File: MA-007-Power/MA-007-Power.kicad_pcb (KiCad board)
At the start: 2 copper layers, 61 x 41.9 mm, 14 parts, among them J1 Conn_01x02, J2 Conn_01x03, J3 Power Out

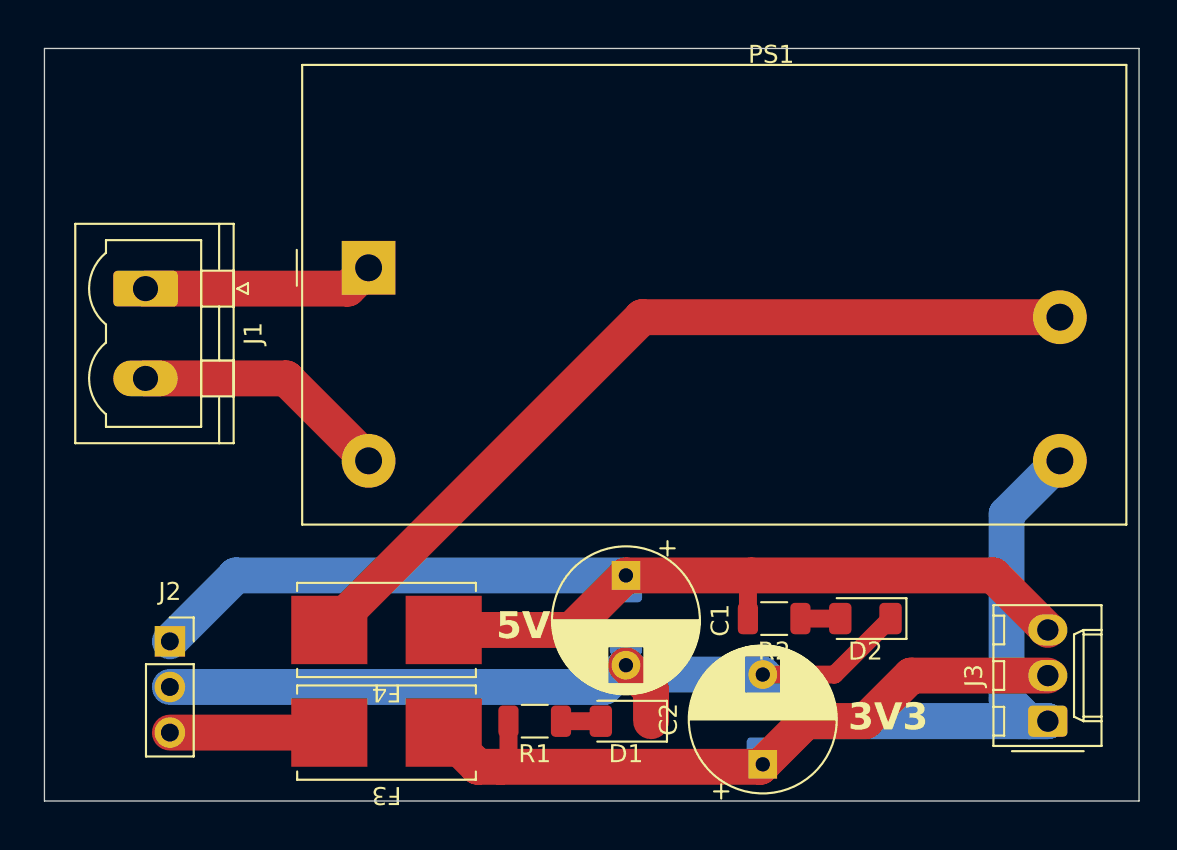
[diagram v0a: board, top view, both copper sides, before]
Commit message: Finished up PCBs, added stencil
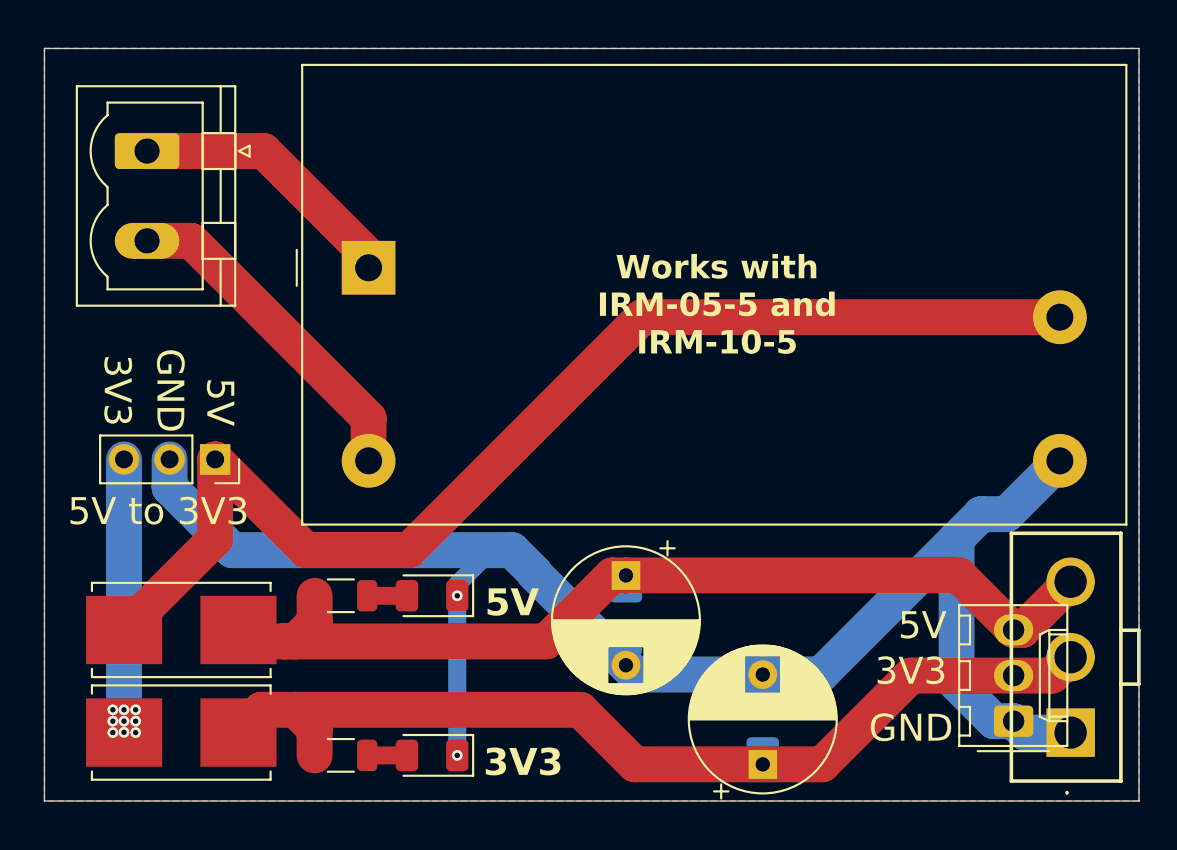
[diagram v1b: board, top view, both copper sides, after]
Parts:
- added J4: 43242-0005, Molex_MiniFitJr_1x3:Molex_MiniFitJr_1x3_PCB, F.Cu at (159.4, 94.0)
- moved D2 24.2 mm to (123.8, 86.4)
- moved R2 24.2 mm to (118.7, 86.4)
- moved F3 11.4 mm to (109.9, 94.0)
- moved F4 11.4 mm to (109.9, 88.3)
- moved D1 11.0 mm to (123.8, 95.2)
- moved R1 11.0 mm to (118.7, 95.2)
- moved J2 10.4 mm to (111.7, 78.8), turned to -90 degrees
- moved J1 7.66 mm to (108.0, 61.6)
- moved J3 1.91 mm to (156.2, 93.3)
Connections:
- J2 pad 1: /5V -> /5V_PRE
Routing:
- net /5V_PRE: track 47.9 -> 66.1 mm
- net /3V3: track 39.3 -> 53.6 mm
- net /5V: track 65.6 -> 54.1 mm
- net GND: track 80.1 -> 88.3 mm, vias 0 -> 2
- net Net-(J2-Pin_3): track 8.88 -> 15.2 mm, vias 0 -> 9
- net Net-(J1-Pin_2): track 14.3 -> 18.8 mm
- net Net-(J1-Pin_1): track 12.9 -> 15.4 mm
- added copper zone on B.Cu, net GND
- added copper zone on F.Cu, net GND
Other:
- board text added: "5V to 3V3"
- board text added: "GND"
- board text added: "MA-507/1 10.25 Jomer.dev"
- board text added: "Works with IRM-05-5 and IRM-10-5"
